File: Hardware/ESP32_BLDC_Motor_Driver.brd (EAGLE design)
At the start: 85.1 x 57.1 mm, 161 parts, among them J1 USB-C Connector, J2 0532610371, J3 POWER_JACKPOWER_JACK_SLOT, J4 Breadboard Connector, J5 Breadboard Headers, J6 0.1in header, J7 QWIIC_RIGHT_ANGLE, J8 Breakout Header, Q1 20V/4.2A/52mΩ/1.4W, Q2 NPN Transistors, U1 TMC6300, U2 OPA344, U3 ESP-WROOM-3232D-NARROW, U4 CH340C, U5 ESD Diode, U6 AP63357, U7 AP2202-ADJ, U8 TMAG5273

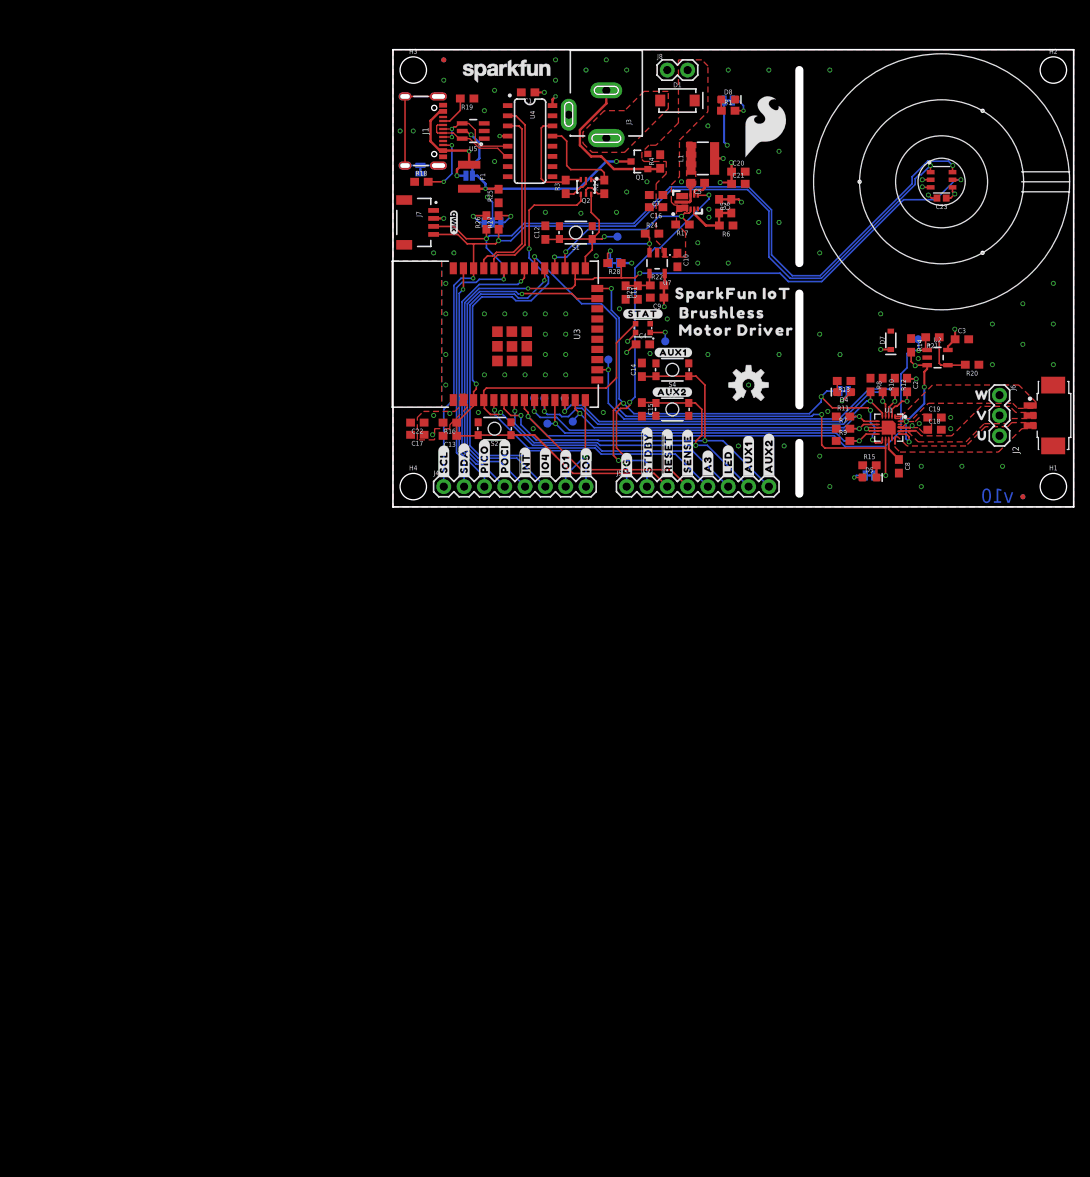
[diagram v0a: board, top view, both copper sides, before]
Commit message: Design Updates
Further work done on inline current sensing - restarting computer
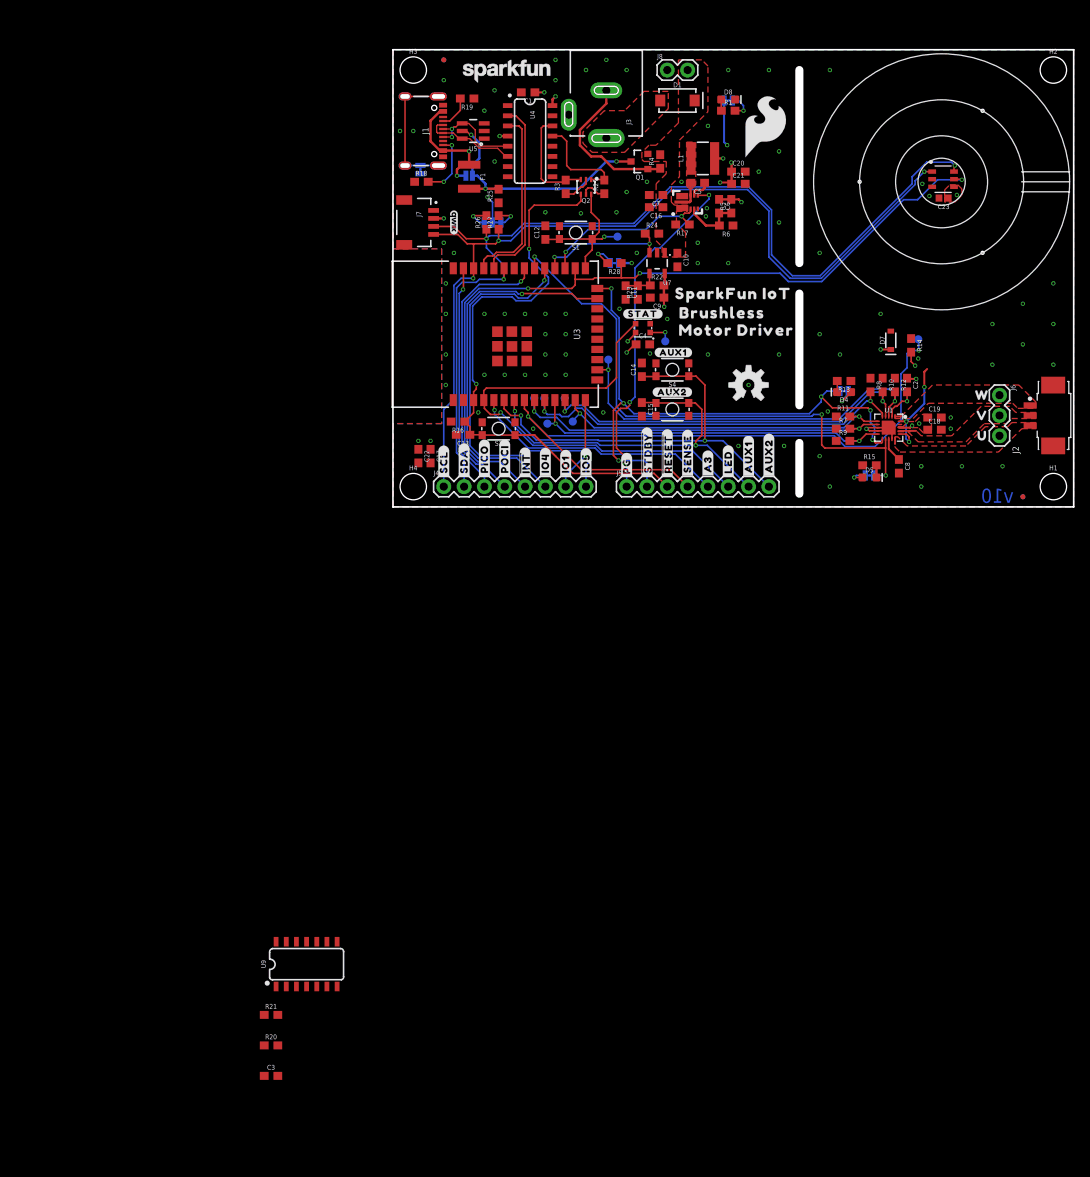
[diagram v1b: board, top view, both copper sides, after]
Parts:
- removed U2: OPA344, SparkFun-IC-Amplifiers:SOT23-5
- added U9: LMV324, SparkFun-IC-Amplifiers:SO14
- moved C3 126.2 mm to (-15.2, -71.1)
- moved R20 122.1 mm to (-15.2, -67.3), turned to 0 degrees
- moved R21 118.4 mm to (-15.2, -63.5), turned to 0 degrees
- moved C22 4.19 mm to (3.17, 6.35), turned to 270 degrees
- moved C17 3.14 mm to (4.70, 6.35), turned to 270 degrees
- moved C13 1.66 mm to (8.76, 9.02)
- moved R16 1.02 mm to (8.13, 10.7)
- moved S2 0.51 mm to (13.2, 9.78)
- moved C23 0.25 mm to (68.8, 38.6)
- moved U8 0.20 mm to (68.8, 41.0)
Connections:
- new net N$14: R20.2, R21.1, U9.3
- net 3.3V_LDO: now also U9.4; no longer U2.5
- net ESP_32/CURR_SENSE: now also U9.1; no longer U2.1
- net GND: now also U9.11; no longer U2.2
- net N$6: now also U9.9; no longer R20.2, R21.1, U2.4
- net SENSE: now also U9.2; no longer U2.3
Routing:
- net N$6: track 6.64 -> 0.00 mm
- net 3.3V_LDO: track 22.4 -> 17.2 mm, vias 14 -> 12
- net ESP_32/CURR_SENSE: track 90.5 -> 87.1 mm
- net GND: track 10.7 -> 7.36 mm, vias 86 -> 85
- net !RESET: track 75.4 -> 73.5 mm
- net SENSE: track 17.0 -> 15.1 mm
- net ESP_22/TP_SCL: track 114.7 -> 113.6 mm
- net N$11: track 3.19 -> 3.80 mm

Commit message: Updates to schematic and layout as per design review checklist
Finished design errors- close to design review
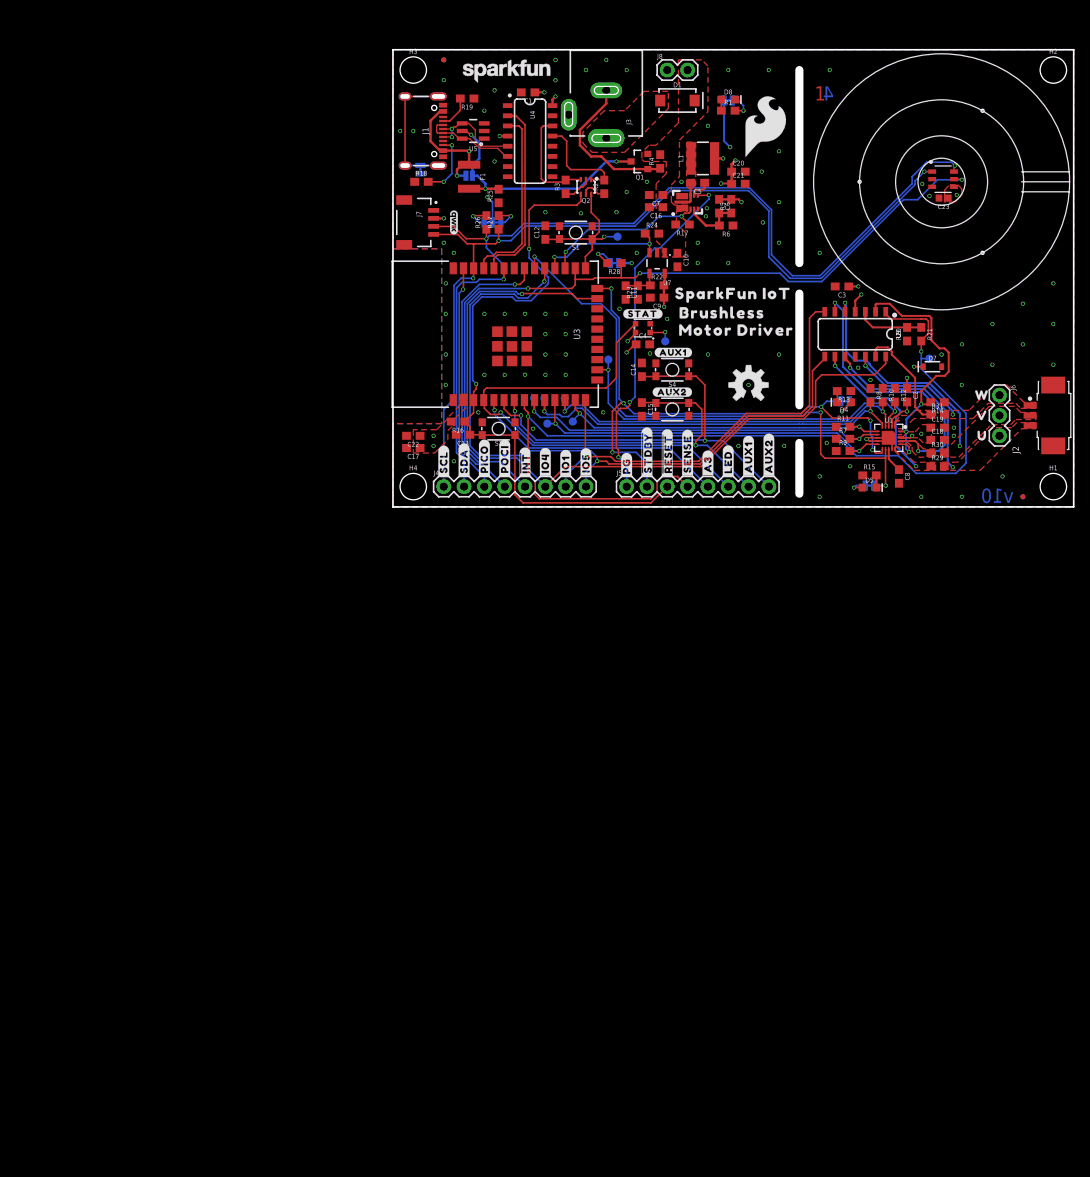
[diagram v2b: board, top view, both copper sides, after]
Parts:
- added R29, R30, R31: 0.015ohm, SparkFun-Resistors:0603
- moved C3 121.8 mm to (56.1, 27.6), turned to 180 degrees
- moved R20 119.3 mm to (64.3, 21.6), turned to 90 degrees
- moved R21 117.7 mm to (66.0, 21.6), turned to 270 degrees
- moved U9 105.3 mm to (58.4, 21.6), turned to 180 degrees
- moved FRAME1 12.7 mm to (19.1, -64.8)
- moved R14 7.84 mm to (68.1, 13.1), turned to 180 degrees
- moved D7 6.17 mm to (67.4, 17.5), turned to 0 degrees
- moved TP9 2.79 mm to (67.1, 18.5), turned to 0 degrees
- moved C22 2.62 mm to (2.54, 8.89), turned to 180 degrees
- moved C17 2.39 mm to (2.54, 7.37), turned to 180 degrees
- moved C18 1.33 mm to (68.1, 8.38)
- moved C19 1.33 mm to (68.1, 9.91)
- moved U$28 1.28 mm to (56.5, 14.9)
- moved S 1.28 mm to (56.5, 13.2)
- moved D4 1.27 mm to (56.4, 13.1)
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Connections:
- removed net ESP_12/GPIO1: J4.7, U3.14
- removed net ESP_15/GPIO4: J4.6, U3.23
- removed net ESP_5/GPIO5: J4.8, U3.29
- removed net N$6: U9.9
- new net ESP_12/V_OUT: J4.7, U3.14, U9.7
- new net ESP_15/W_OUT: J4.6, U3.23, U9.14
- new net ESP_5/U_OUT: J4.8, U3.29, U9.8
- new net SENSE_U: R29.1, U1.15, U9.9
- new net SENSE_V: R30.1, U1.17, U9.6
- new net SENSE_W: R31.1, U1.1, U9.13
- net U: now also R29.2, U9.10; no longer U1.15
- net V: now also R30.2, U9.5; no longer U1.17
- net W: now also R31.2, U9.12; no longer U1.1
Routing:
- net ESP_15/W_OUT: track 0.00 -> 98.7 mm, vias 0 -> 1
- net ESP_5/U_OUT: track 0.00 -> 88.3 mm, vias 0 -> 2
- net ESP_12/V_OUT: track 0.00 -> 56.2 mm, vias 0 -> 1
- net ESP_5/GPIO5: track 50.6 -> 0.00 mm, vias 1 -> 0
- net ESP_15/GPIO4: track 47.0 -> 0.00 mm, vias 1 -> 0
- net SENSE_V: track 0.00 -> 35.5 mm, vias 0 -> 2
- net ESP_32/CURR_SENSE: track 87.1 -> 119.8 mm
- net V: track 2.16 -> 28.9 mm, vias 0 -> 2
- net U: track 0.65 -> 23.3 mm, vias 0 -> 2
- net SENSE_U: track 0.00 -> 20.5 mm, vias 0 -> 2
- net SENSE: track 15.1 -> 33.7 mm, vias 4 -> 3
- net SENSE_W: track 0.00 -> 14.8 mm
- net W: track 0.73 -> 14.8 mm, vias 0 -> 2
- net ESP_12/GPIO1: track 11.8 -> 0.00 mm, vias 1 -> 0
- net N$14: track 0.00 -> 8.39 mm
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- added copper zone on layer 1, net SENSE_U
- added copper zone on layer 1, net SENSE_V
- added copper zone on layer 1, net SENSE_W
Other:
- board text added: "1"
- board text added: "2"
- board text added: "3"
- board text added: "4"

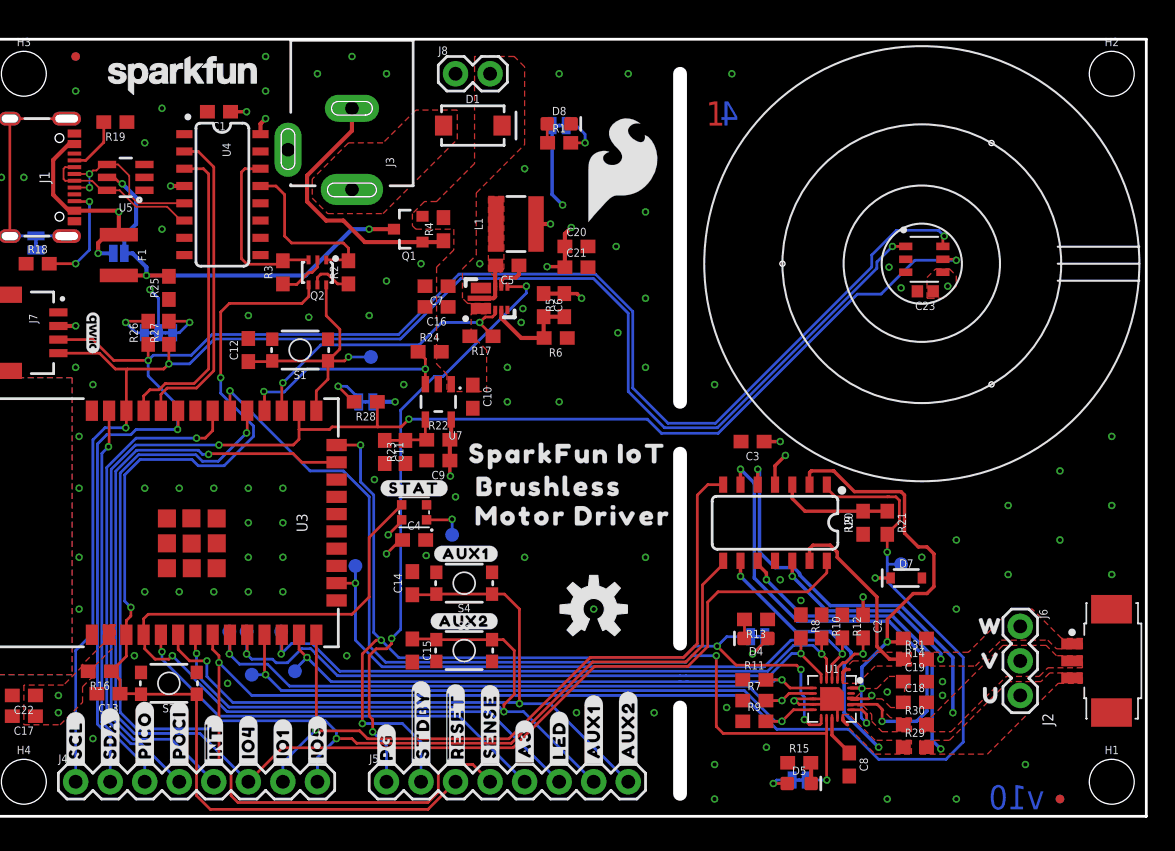
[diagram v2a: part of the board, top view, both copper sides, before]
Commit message: Updates for Design Review
Added more silk for buttons and outputs; added datasheet for correct Op Amp and deleted the old one; adjusted MOLEX output connector to motor for better connectivity and less strain on the cable; changed version number to v01; added more GND vias
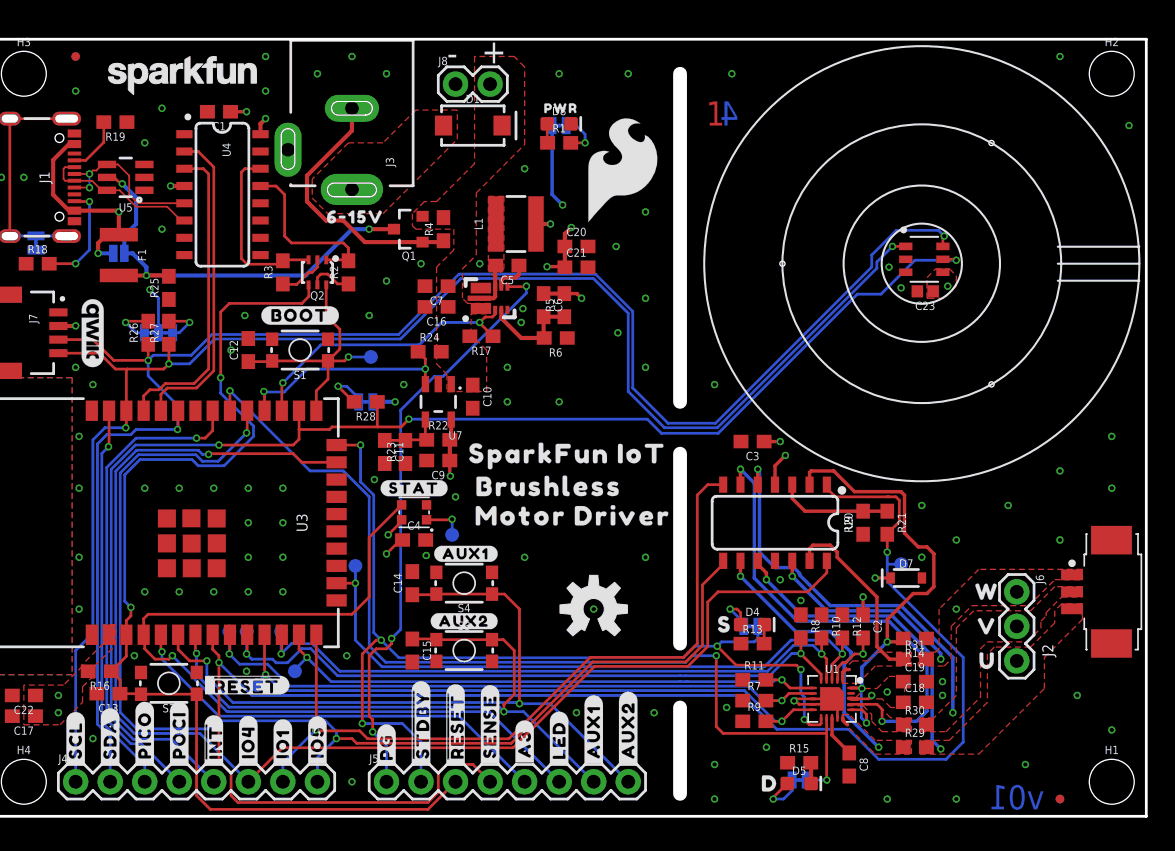
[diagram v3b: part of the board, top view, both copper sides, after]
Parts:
- added U$52: (no value), output:S630063003507
- added U$53: (no value), output:D630063003508
- added U$54: (no value), output:#_#RESET#630063003486
- added U$55: (no value), output:6#15V630063003510
- added U$56: (no value), output:PWR3441
- added U$57: (no value), output:U630063003494
- added U$58: (no value), output:#BOOT#630063003512
- added U$59: (no value), output:SPARKFUN_IOT_BRUSHLESS630063003514
- added U$60: (no value), output:V630063003496
- added U$61: (no value), output:W630063003497
- added U$62: (no value), output:MOTOR_DRIVER630063003515
- LOGO4: value QWIIC_LOGO_3MM -> QWIIC_LOGO_5MM; device SparkFun-Aesthetics:QWIIC_3MM -> SparkFun-Aesthetics:QWIIC_5MM
- moved J2 5.08 mm to (79.6, 16.5)
- moved U$24 3.81 mm to (3.30, 40.3)
- moved J6 2.55 mm to (75.6, 16.5)
- moved U$50 2.55 mm to (73.4, 14.0)
- moved U$51 2.55 mm to (73.4, 16.5)
- moved U$49 2.55 mm to (73.4, 11.4)
- moved R13 1.80 mm to (56.1, 12.7), turned to 0 degrees
- moved D4 1.05 mm to (56.1, 14.1), turned to 0 degrees
- moved S 0.92 mm to (56.0, 14.0), turned to 180 degrees
- moved U$28 0.92 mm to (56.0, 15.6)
- moved TP6 0.85 mm to (19.7, 9.65)
- moved J8 0.76 mm to (34.3, 53.8)
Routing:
- net D: track 2.52 -> 3.99 mm
- net ESP_0/!STDBY: track 72.3 -> 73.7 mm
- net GND: vias 88 -> 92
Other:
- board text added: "+"
- board text added: "-"
- board text added: "v01"
- board text removed: "v10"
